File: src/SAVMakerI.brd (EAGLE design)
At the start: 53.3 x 53.3 mm, 50 parts, among them J2 AVR_SPI_PRG_6PTH, Q1 CSM-3X-CRYSTALCSM-3X, U1 ATMEGA32U4-AU

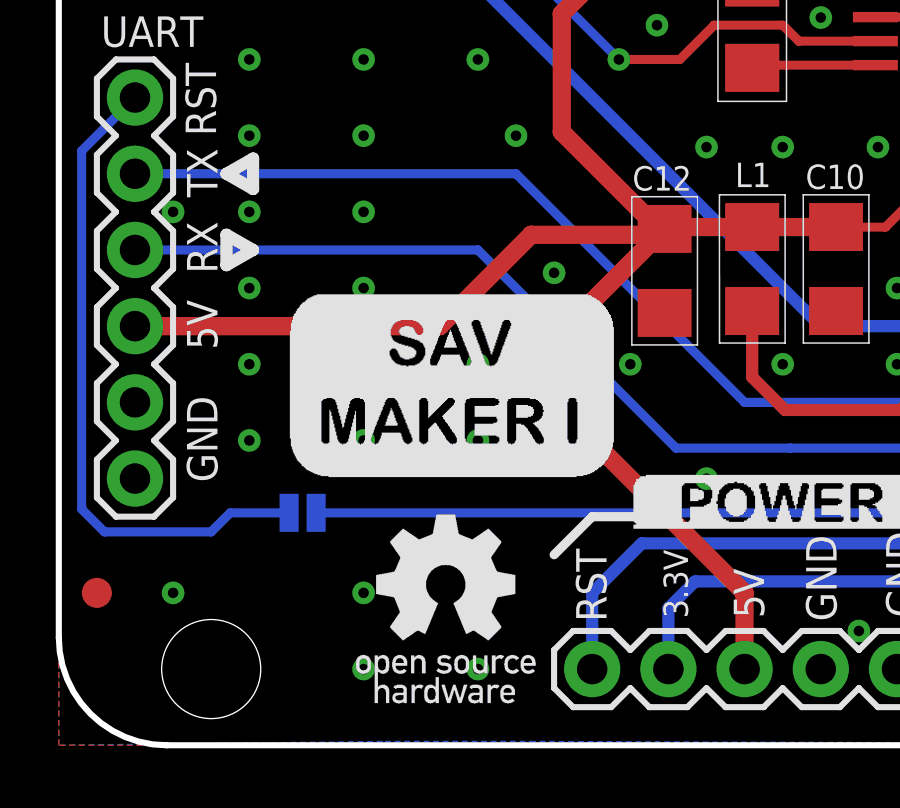
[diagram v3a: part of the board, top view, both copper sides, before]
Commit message: Updated documentation: schematic and 3D renders.
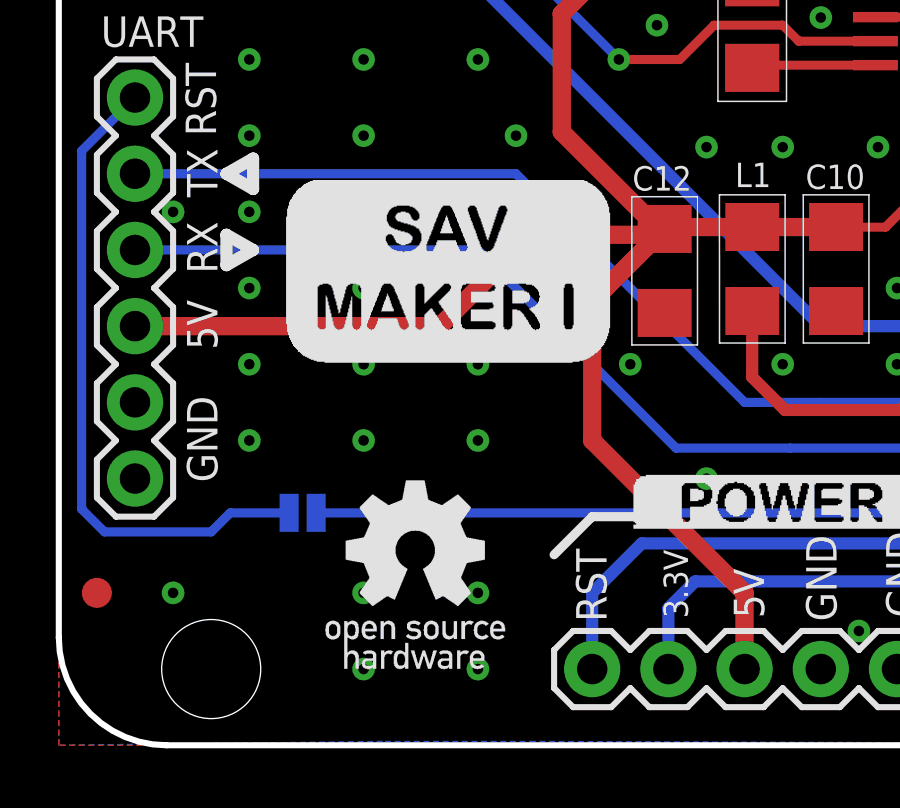
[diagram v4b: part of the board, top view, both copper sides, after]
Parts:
- moved U$10 3.81 mm to (7.49, 12.7)
- moved U$13 1.53 mm to (8.89, 2.54)
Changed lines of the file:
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@@
 <layer number="14" name="Route14" color="1" fill="6" visible="no" active="no"/>
 <layer number="15" name="Route15" color="4" fill="6" visible="no" active="no"/>
-<layer number="16" name="Bottom" color="1" fill="1" visible="no" active="yes"/>
+<layer number="16" name="Bottom" color="1" fill="1" visible="yes" active="yes"/>
 <layer number="17" name="Pads" color="2" fill="1" visible="yes" active="yes"/>
 <layer number="18" name="Vias" color="2" fill="1" visible="yes" active="yes"/>
@@
 <element name="U$5" library="SparkFun" package="STAND-OFF" value="" x="5.08" y="2.54"/>
 <element name="U$9" library="fmc" package="ELECTROFUN_STRIP" value="" x="46.99" y="7.62" rot="MR0"/>
-<element name="U$10" library="SAVMakerI" package="SAVMAKERI" value="" x="7.62" y="8.89"/>
+<element name="U$10" library="SAVMakerI" package="SAVMAKERI" value="" x="7.493" y="12.7"/>
 <element name="U$16" library="SAVMakerI" package="ANALOG_BMP" value="" x="36.068" y="7.112"/>
 <element name="U$17" library="SAVMakerI" package="DIGITAL_BMP" value="" x="22.987" y="42.545"/>
 <element name="U$18" library="SAVMakerI" package="POWER_BMP" value="" x="19.177" y="7.239"/>
-<element name="U$13" library="SAVMakerI" package="OSHW" value="" x="9.906" y="1.397"/>
+<element name="U$13" library="SAVMakerI" package="OSHW" value="" x="8.89" y="2.54"/>
 <element name="B" library="fmc" package="BOARD_INFO_BMP" value="SAV Maker I" x="36.83" y="24.13" rot="MR0"/>
 <element name="U$14" library="fmc" package="CERN_OHL" value="" x="36.83" y="17.78" rot="MR0"/>
